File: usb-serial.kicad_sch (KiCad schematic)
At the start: 8 parts, among them J6 USB_C_Receptacle, U23 USBLC6-2SC6, U24 CH340G, Y3 12MHz

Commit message: Updated MCU to MCU module + set SMD comp. footprints
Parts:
- C46, C47: footprint (none) -> Capacitor_SMD:C_0603_1608Metric
- Y3: footprint (none) -> Crystal:Crystal_SMD_3225-4Pin_3.2x2.5mm
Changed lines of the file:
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@@
 			)
 		)
-		(property "Footprint" ""
+		(property "Footprint" "Capacitor_SMD:C_0603_1608Metric"
 			(at 155.9052 96.52 0)
 			(effects
@@
 			)
 		)
-		(property "Footprint" ""
+		(property "Footprint" "Capacitor_SMD:C_0603_1608Metric"
 			(at 143.2052 96.52 0)
 			(effects
@@
 			)
 		)
-		(property "Footprint" ""
+		(property "Footprint" "Crystal:Crystal_SMD_3225-4Pin_3.2x2.5mm"
 			(at 148.59 73.66 0)
 			(effects

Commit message: updated silk + started routing
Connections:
- net GND: now also Y3.2, Y3.4
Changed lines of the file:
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@@
+	)
+	(junction
+		(at 137.16 80.01)
+		(diameter 0)
+		(color 0 0 0 0)
 	)
 	(junction
@@
 	(junction
 		(at 142.24 73.66)
+		(diameter 0)
+		(color 0 0 0 0)
+	)
+	(junction
+		(at 142.24 97.79)
 		(diameter 0)
 		(color 0 0 0 0)
@@
 	(wire
 		(pts
+			(xy 148.59 66.04) (xy 148.59 68.58)
+		)
+		(stroke
+			(width 0)
+			(type default)
+		)
+	)
+	(wire
+		(pts
 			(xy 149.86 54.61) (xy 152.4 52.07)
 		)
@@
 		)
 	)
+	(wire
+		(pts
+			(xy 137.16 80.01) (xy 148.59 80.01)
+		)
+		(stroke
+			(width 0)
+			(type default)
+		)
+	)
 	(bus
 		(pts
@@
 	(wire
 		(pts
+			(xy 148.59 66.04) (xy 137.16 66.04)
+		)
+		(stroke
+			(width 0)
+			(type default)
+		)
+	)
+	(wire
+		(pts
 			(xy 102.87 43.18) (xy 101.6 43.18)
 		)
@@
 	(wire
 		(pts
+			(xy 142.24 97.79) (xy 142.24 96.52)
+		)
+		(stroke
+			(width 0)
+			(type default)
+		)
+	)
+	(wire
+		(pts
 			(xy 173.99 73.66) (xy 173.99 69.85)
 		)
@@
 	(wire
 		(pts
-			(xy 142.24 99.06) (xy 142.24 96.52)
+			(xy 142.24 99.06) (xy 142.24 97.79)
 		)
 		(stroke
@@
 	(wire
 		(pts
+			(xy 137.16 66.04) (xy 137.16 80.01)
+		)
+		(stroke
+			(width 0)
+			(type default)
+		)
+	)
+	(wire
+		(pts
 			(xy 184.15 46.99) (xy 198.12 46.99)
 		)
@@
 	(wire
 		(pts
+			(xy 137.16 80.01) (xy 137.16 97.79)
+		)
+		(stroke
+			(width 0)
+			(type default)
+		)
+	)
+	(wire
+		(pts
 			(xy 71.12 102.87) (xy 71.12 109.22)
 		)
@@
 		)
 	)
+	(wire
+		(pts
+			(xy 148.59 80.01) (xy 148.59 78.74)
+		)
+		(stroke
+			(width 0)
+			(type default)
+		)
+	)
 	(bus
 		(pts
@@
 		)
 		(stroke
+			(width 0)
+			(type default)
+		)
+	)
+	(wire
+		(pts
+			(xy 137.16 97.79) (xy 142.24 97.79)
+		)
+		(stroke

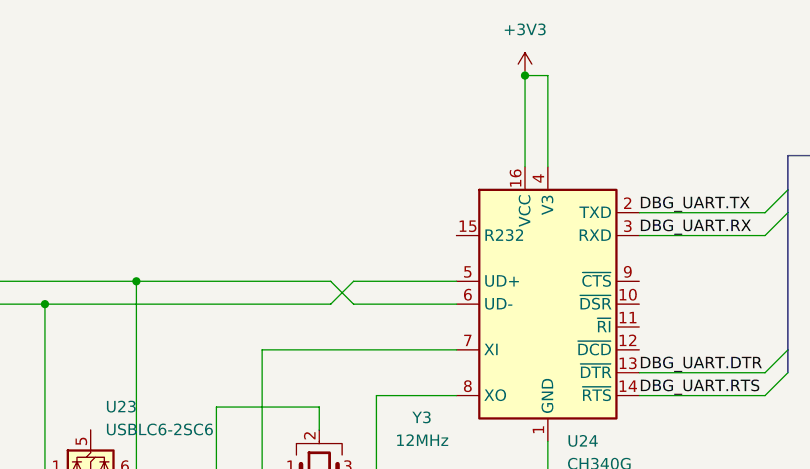
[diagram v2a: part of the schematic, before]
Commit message: finished routing SPI, I2C and MikroBUS
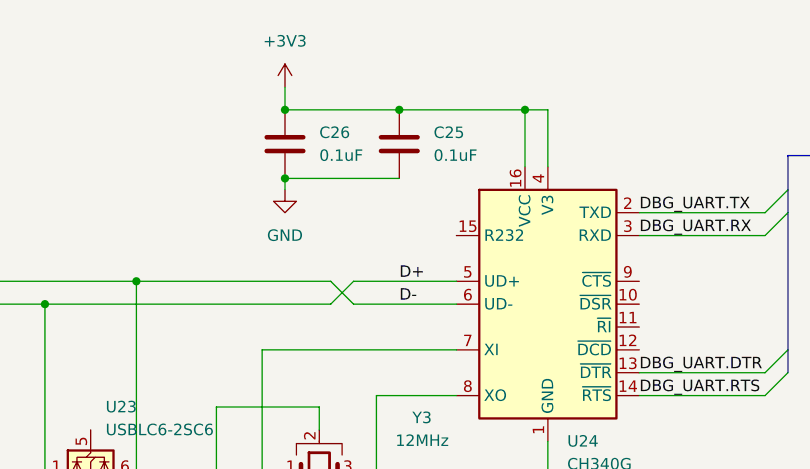
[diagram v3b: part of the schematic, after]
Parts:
- added C25, C26: 0.1uF, Capacitor_SMD:C_0603_1608Metric, symbol Device:C
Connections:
- net +3V3: now also C25.1, C26.1
- net GND: now also C25.2, C26.2
- net D+: now reaches J6.A6 (D+), J6.B6 (D+), U23.1 (I/O1), U24.5 (UD+)
- net D-: now reaches J6.A7 (D-), J6.B7 (D-), U23.6 (I/O1), U24.6 (UD-)
